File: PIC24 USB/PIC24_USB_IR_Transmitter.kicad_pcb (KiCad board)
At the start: 2 copper layers, 86.4 x 48.3 mm, 64 parts, among them CON1 USB-MINI-B, P1 CONN_6, P2 CONN_4, P3 CONN_4, P4 CONN_8, P5 CONN_4, P6 CONN_1, P7 CONN_8, P8 CONN_8X2, Q1 2N7002, Q2 2N7002, Q3 2N7002, Q4 2N7002, Q5 2N7002, Q6 2N7002, U1 PIC24FJXXXGB106, U2 LM1117_SOT223_3V3, U3 50mm_5x7_Dot_Matrix_Led_Displ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, U4 MCP48X2, U5 MCP9700, U6 24C16, U7 TCN75, X1 CRYSTAL_12MHZ, X2 32khz

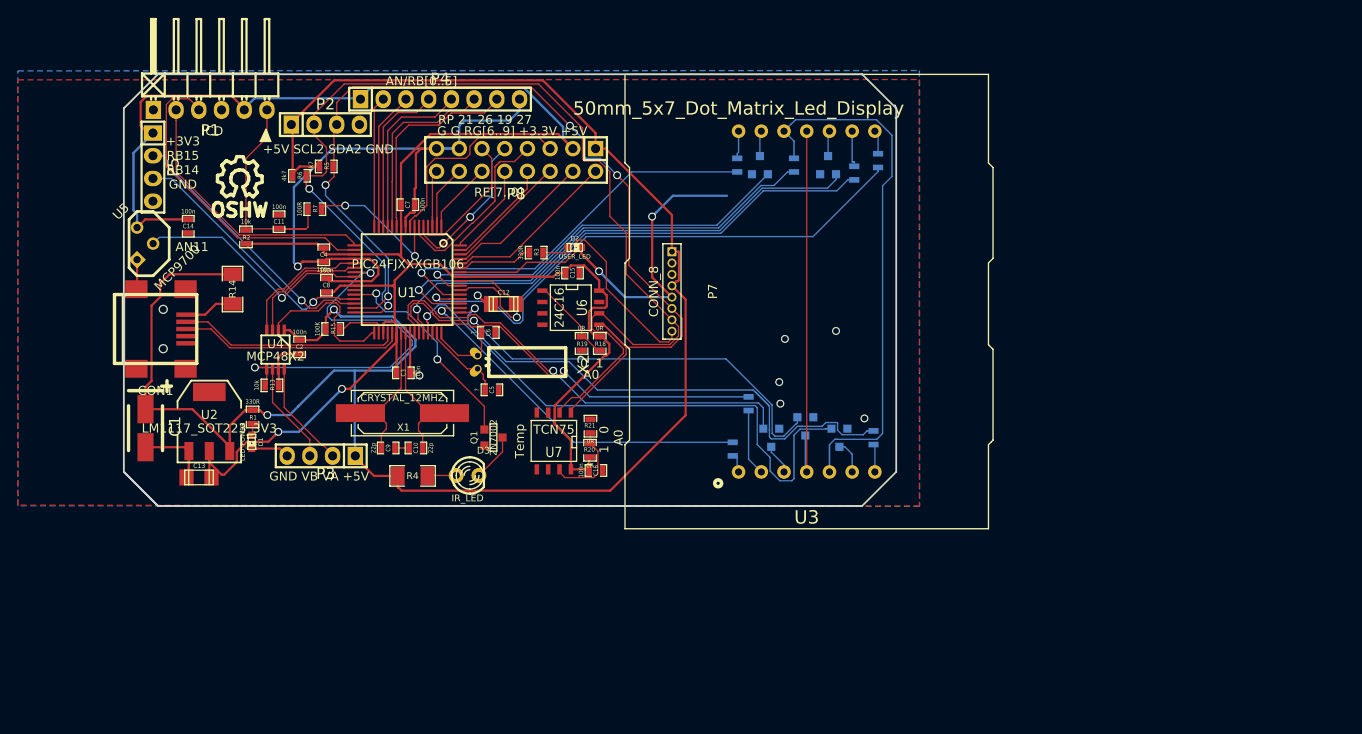
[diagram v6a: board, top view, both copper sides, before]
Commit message: minor changes: fixed outline, fixed collision
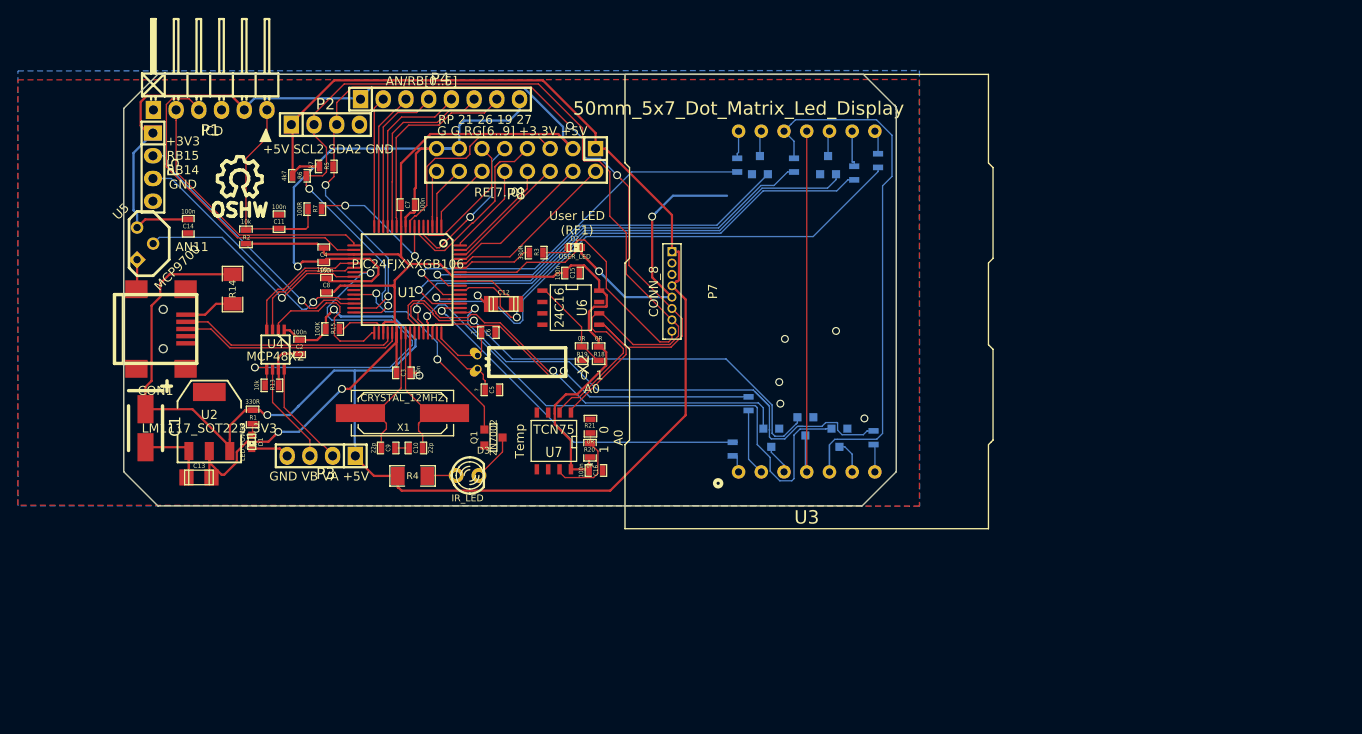
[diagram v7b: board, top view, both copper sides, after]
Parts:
- moved R18 1.15 mm to (77.2, 43.9)
- moved R19 1.14 mm to (75.3, 43.9)
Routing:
- net +3.3V: track 241.7 -> 240.6 mm
- net Net-(R18-Pad2): track 9.81 -> 10.8 mm
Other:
- outline, holes or cut-outs redrawn
- board text added: "User LED (RF1)"
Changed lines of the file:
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@@
-(kicad_pcb (version 4) (host pcbnew "(2014-09-14 BZR 5132)-product")
+(kicad_pcb (version 4) (host pcbnew 0.201411151246+5284~19~ubuntu14.04.1-product)
   (general
     (links 186)
     (no_connects 1)
-    (area 24.029999 12.599999 110.590001 61.060001)
+    (area 24.054999 12.624999 110.565001 61.035001)
     (thickness 1.6)
-    (drawings 38)
-    (tracks 955)
+    (drawings 39)
+    (tracks 956)
     (zones 0)
     (modules 64)
@@
   )
   (module SMD_Packages:SMD-0603_r (layer F.Cu)
-    (at 77.343 42.799 270)
+    (at 77.216 43.942 270)
     (attr smd)
     (fp_text reference R18 (at 0.0635 -0.0635 360) (layer F.SilkS)
@@
   )
   (module SMD_Packages:SMD-0603_r (layer F.Cu)
-    (at 75.311 42.799 270)
+    (at 75.311 43.942 270)
     (attr smd)
     (fp_text reference R19 (at 0.0635 -0.0635 360) (layer F.SilkS)
@@
     )
   )
+  (gr_line (start 24.13 16.51) (end 24.13 57.15) (angle 90) (layer Edge.Cuts) (width 0.15))
+  (gr_line (start 27.94 12.7) (end 24.13 16.51) (angle 90) (layer Edge.Cuts) (width 0.15))
+  (gr_line (start 106.807 12.7) (end 27.94 12.7) (angle 90) (layer Edge.Cuts) (width 0.15))
+  (gr_line (start 110.49 16.383) (end 106.807 12.7) (angle 90) (layer Edge.Cuts) (width 0.15))
+  (gr_line (start 110.49 16.637) (end 110.49 16.383) (angle 90) (layer Edge.Cuts) (width 0.15))
+  (gr_line (start 110.49 17.018) (end 110.49 16.637) (angle 90) (layer Edge.Cuts) (width 0.15))
+  (gr_line (start 110.49 57.15) (end 110.49 17.018) (angle 90) (layer Edge.Cuts) (width 0.15))
+  (gr_line (start 106.68 60.96) (end 110.49 57.15) (angle 90) (layer Edge.Cuts) (width 0.15))
+  (gr_line (start 27.94 60.96) (end 106.68 60.96) (angle 90) (layer Edge.Cuts) (width 0.15))
+  (gr_line (start 24.13 57.15) (end 27.94 60.96) (angle 90) (layer Edge.Cuts) (width 0.15))
+  (gr_text "User LED\n(RF1)" (at 74.803 29.337) (layer F.SilkS)
+    (effects (font (size 1 1) (thickness 0.25)))
+  )
   (gr_text "1   0\n A0 " (at 78.6384 53.5432 90) (layer F.SilkS)
     (effects (font (size 1 1) (thickness 0.25)))
@@
     (effects (font (size 1 1) (thickness 0.25)))
   )
-  (gr_text "0  1" (at 76.454 45.0215) (layer F.SilkS)
+  (gr_text "0  1" (at 76.454 46.355) (layer F.SilkS)
     (effects (font (size 1 1) (thickness 0.25)))
   )
-  (gr_text A0 (at 76.3905 46.2915) (layer F.SilkS)
+  (gr_text A0 (at 76.454 47.879) (layer F.SilkS)
     (effects (font (size 1 1) (thickness 0.25)))
   )
@@
     (effects (font (size 1 1) (thickness 0.25)))
   )
-  (gr_line (start 24.13 57.15) (end 27.94 60.96) (layer Edge.Cuts) (width 0.2))
-  (gr_line (start 24.13 16.51) (end 24.13 57.15) (layer Edge.Cuts) (width 0.2))
-  (gr_line (start 27.94 12.7) (end 24.13 16.51) (layer Edge.Cuts) (width 0.2))
-  (gr_line (start 106.68 12.7) (end 27.94 12.7) (layer Edge.Cuts) (width 0.2))
-  (gr_line (start 110.49 16.51) (end 106.68 12.7) (layer Edge.Cuts) (width 0.2))
-  (gr_line (start 110.49 57.15) (end 110.49 16.51) (layer Edge.Cuts) (width 0.2))
-  (gr_line (start 106.68 60.96) (end 110.49 57.15) (layer Edge.Cuts) (width 0.2))
-  (gr_line (start 27.94 60.96) (end 106.68 60.96) (layer Edge.Cuts) (width 0.2))
-  (gr_line (start 24.13 57.15) (end 27.94 60.96) (layer Edge.Cuts) (width 0.2))
   (dimension 48.26 (width 0.25) (layer Dwgs.User)
     (gr_text "48,260 mm" (at 12.97 36.83 270) (layer Dwgs.User)
@@
     (arrow2b (pts (xy 24.13 69.85) (xy 25.256504 69.263579)))
   )
-  (gr_line (start 106.68 60.96) (end 27.94 60.96) (angle 90) (layer Edge.Cuts) (width 0.15))
   (gr_line (start 40.019 19.684) (end 40.519 20.184) (layer F.SilkS) (width 0.2))
   (gr_line (start 39.819 19.884) (end 40.019 19.684) (layer F.SilkS) (width 0.2))
@@
   (via (at 106.934 51.181) (size 0.889) (drill 0.635) (layers F.Cu B.Cu) (net 0))
   (via (at 97.409 47.117) (size 0.889) (drill 0.635) (layers F.Cu B.Cu) (net 0))
-  (segment (start 76.577698 38.8112) (end 77.955902 38.8112) (width 0.254) (layer F.Cu) (net 1))
-  (segment (start 77.955902 38.8112) (end 78.128001 38.639101) (width 0.254) (layer F.Cu) (net 1))
-  (segment (start 78.128001 38.639101) (end 78.128001 37.424501) (width 0.254) (layer F.Cu) (net 1))
+  (segment (start 77.216 43.18) (end 77.216 42.368318) (width 0.254) (layer F.Cu) (net 1))
+  (segment (start 77.216 42.368318) (end 76.130989 41.283308) (width 0.254) (layer F.Cu) (net 1))
+  (segment (start 76.694397 38.694501) (end 78.072601 38.694501) (width 0.254) (layer F.Cu) (net 1))
   (segment (start 78.128001 37.424501) (end 77.597 36.8935) (width 0.254) (layer F.Cu) (net 1))
-  (segment (start 77.597 36.8935) (end 77.2795 36.8935) (width 0.254) (layer F.Cu) (net 1))
   (segment (start 76.130989 41.283308) (end 76.130989 39.257909) (width 0.254) (layer F.Cu) (net 1))
-  (segment (start 76.130989 39.257909) (end 76.577698 38.8112) (width 0.254) (layer F.Cu) (net 1))
+  (segment (start 77.597 36.8935) (end 77.2795 36.8935) (width 0.254) (layer F.Cu) (net 1))
+  (segment (start 76.130989 39.257909) (end 76.694397 38.694501) (width 0.254) (layer F.Cu) (net 1))
+  (segment (start 78.072601 38.694501) (end 78.128001 38.639101) (width 0.254) (layer F.Cu) (net 1))
+  (segment (start 78.128001 38.639101) (end 78.128001 37.424501) (width 0.254) (layer F.Cu) (net 1))
+  (segment (start 72.316199 50.065457) (end 72.316199 50.683691) (width 0.254) (layer F.Cu) (net 1))
+  (segment (start 72.316199 50.683691) (end 72.316199 51.831099) (width 0.254) (layer F.Cu) (net 1))
+  (segment (start 77.216 43.18) (end 77.47 43.18) (width 0.254) (layer F.Cu) (net 1))
+  (segment (start 78.064501 45.243101) (end 74.815412 48.49219) (width 0.254) (layer F.Cu) (net 1))
+  (segment (start 77.47 43.18) (end 78.064501 43.774501) (width 0.254) (layer F.Cu) (net 1))
+  (segment (start 78.064501 43.774501) (end 78.064501 45.243101) (width 0.254) (layer F.Cu) (net 1))
+  (segment (start 74.815412 48.49219) (end 73.551508 48.49219) (width 0.254) (layer F.Cu) (net 1))
+  (segment (start 73.551508 48.49219) (end 72.316199 49.727499) (width 0.254) (layer F.Cu) (net 1))
+  (segment (start 72.316199 49.727499) (end 72.316199 50.683691) (width 0.254) (layer F.Cu) (net 1))
   (segment (start 77.2795 35.759898) (end 75.596101 34.076499) (width 0.254) (layer F.Cu) (net 1))
   (segment (start 77.2795 36.8935) (end 77.2795 35.759898) (width 0.254) (layer F.Cu) (net 1))
   (segment (start 77.2795 36.8935) (end 76.962 36.8935) (width 0.254) (layer F.Cu) (net 1))
-  (segment (start 76.130989 41.283308) (end 76.884681 42.037) (width 0.254) (layer F.Cu) (net 1))
-  (segment (start 76.884681 42.037) (end 77.343 42.037) (width 0.254) (layer F.Cu) (net 1))
   (segment (start 76.1492 56.9976) (end 76.1492 55.6006) (width 0.254) (layer F.Cu) (net 1))
   (segment (start 76.1492 55.6006) (end 76.2508 55.499) (width 0.254) (layer F.Cu) (net 1))
@@
   (segment (start 74.1172 53.6321) (end 72.316199 51.831099) (width 0.254) (layer F.Cu) (net 1))
   (segment (start 74.1172 56.8706) (end 74.1172 53.6321) (width 0.254) (layer F.Cu) (net 1))
-  (segment (start 72.316199 49.727499) (end 72.316199 51.831099) (width 0.254) (layer F.Cu) (net 1))
-  (segment (start 72.316199 50.065457) (end 72.316199 51.831099) (width 0.254) (layer F.Cu) (net 1))
-  (segment (start 78.094699 44.155501) (end 77.888197 44.155501) (width 0.254) (layer F.Cu) (net 1))
-  (segment (start 78.4098 43.8404) (end 78.094699 44.155501) (width 0.254) (layer F.Cu) (net 1))
-  (segment (start 77.888197 44.155501) (end 72.316199 49.727499) (width 0.254) (layer F.Cu) (net 1))
-  (segment (start 78.4098 42.8498) (end 78.4098 43.8404) (width 0.254) (layer F.Cu) (net 1))
-  (segment (start 77.343 42.037) (end 77.597 42.037) (width 0.254) (layer F.Cu) (net 1))
-  (segment (start 77.597 42.037) (end 78.4098 42.8498) (width 0.254) (layer F.Cu) (net 1))
   (segment (start 75.651501 34.131899) (end 75.596101 34.076499) (width 0.254) (layer F.Cu) (net 1))
   (segment (start 74.127501 34.076499) (end 73.533 34.671) (width 0.254) (layer F.Cu) (net 1))
@@
   (segment (start 105.7775 22.506) (end 105.791 22.5195) (width 0.15) (layer B.Cu) (net 76))
   (segment (start 105.564 22.506) (end 105.7775 22.506) (width 0.15) (layer B.Cu) (net 76))
-  (segment (start 77.343 43.561) (end 77.089 43.561) (width 0.15) (layer F.Cu) (net 77))
-  (segment (start 77.089 43.561) (end 75.565 42.037) (width 0.15) (layer F.Cu) (net 77))
-  (segment (start 75.565 42.037) (end 75.311 42.037) (width 0.15) (layer F.Cu) (net 77))
-  (segment (start 75.311 42.037) (end 75.311 40.9575) (width 0.15) (layer F.Cu) (net 77))
+  (segment (start 75.311 43.18) (end 75.565 43.18) (width 0.15) (layer F.Cu) (net 77))
+  (segment (start 75.565 43.18) (end 77.089 44.704) (width 0.15) (layer F.Cu) (net 77))
+  (segment (start 77.089 44.704) (end 77.216 44.704) (width 0.15) (layer F.Cu) (net 77))
+  (segment (start 75.311 43.18) (end 75.311 40.9575) (width 0.15) (layer F.Cu) (net 77))
   (segment (start 75.311 40.9575) (end 71.247 36.8935) (width 0.15) (layer F.Cu) (net 77))
   (segment (start 71.247 36.8935) (end 70.9295 36.8935) (width 0.15) (layer F.Cu) (net 77))

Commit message: Updated
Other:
- board text added: "(cc) bittenbybytes 2015 PIC 24/32 LQFP64 USB dev board"
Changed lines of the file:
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@@
-(kicad_pcb (version 4) (host pcbnew 0.201411151246+5284~19~ubuntu14.04.1-product)
+(kicad_pcb (version 4) (host pcbnew 4.0.0-1rc2.201511201506+6189~38~ubuntu14.04.1-stable)
   (general
     (links 186)
@@
     (area 24.054999 12.624999 110.565001 61.035001)
     (thickness 1.6)
-    (drawings 39)
+    (drawings 40)
     (tracks 956)
     (zones 0)
@@
       (linewidth 0.150000)
       (plotframeref false)
-      (viasonmask false)
+      (viasonmask true)
       (mode 1)
       (useauxorigin false)
@@
     )
   )
+  (gr_text "(cc) bittenbybytes 2015\nPIC 24/32 LQFP64 USB dev board" (at 41.402 58.4835 180) (layer B.SilkS)
+    (effects (font (size 1 1) (thickness 0.25)) (justify mirror))
+  )
   (gr_line (start 24.13 16.51) (end 24.13 57.15) (angle 90) (layer Edge.Cuts) (width 0.15))
